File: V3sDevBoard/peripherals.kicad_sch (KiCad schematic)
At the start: 7 parts, among them Q1 NPN, Q2 PNP

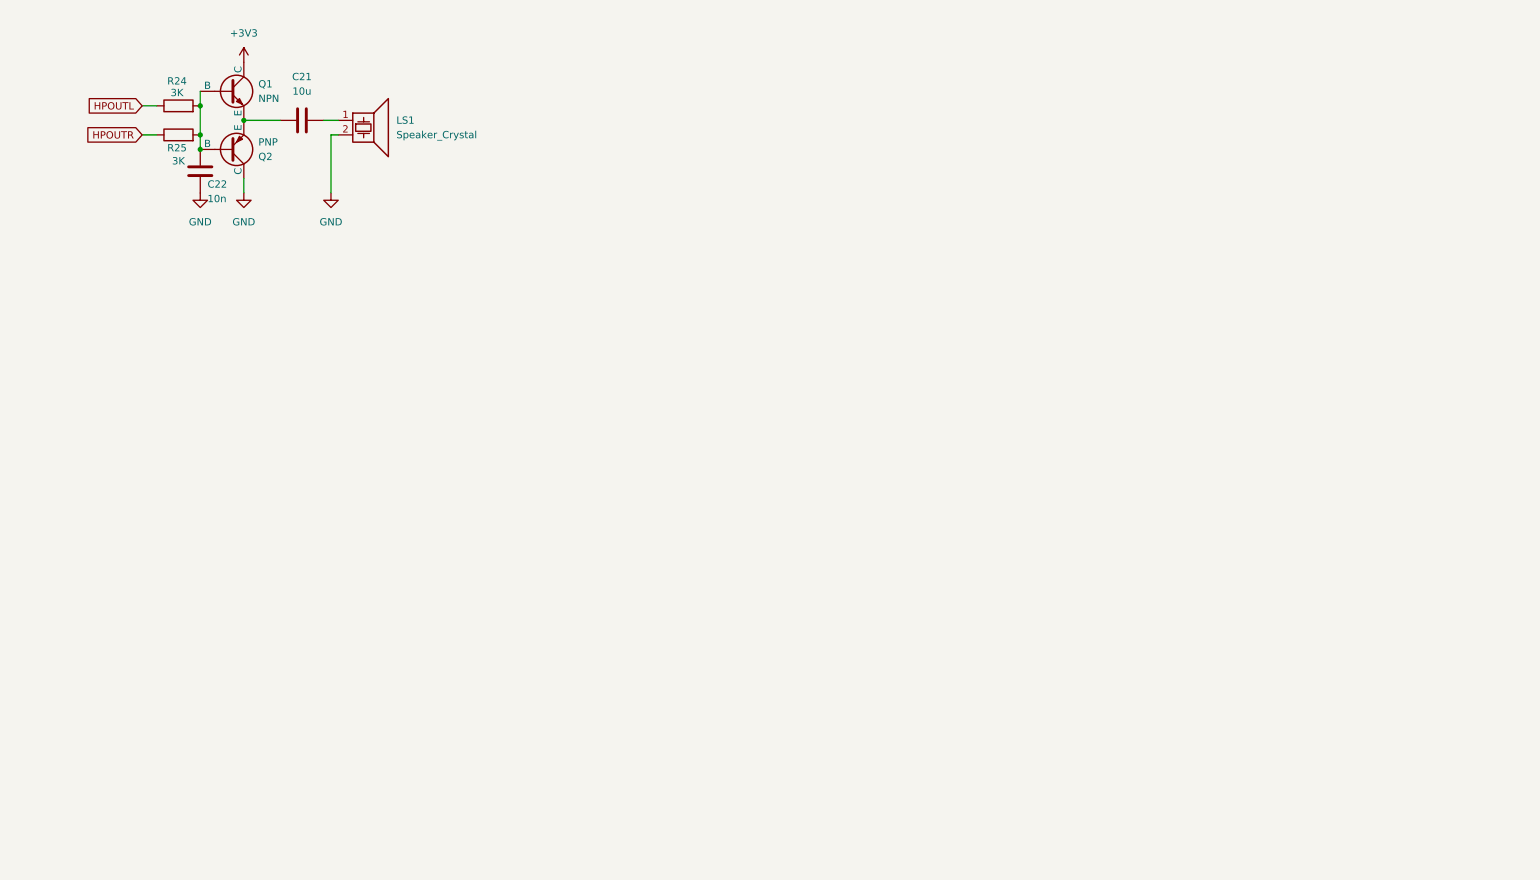
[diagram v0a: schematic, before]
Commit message: drawing schematics
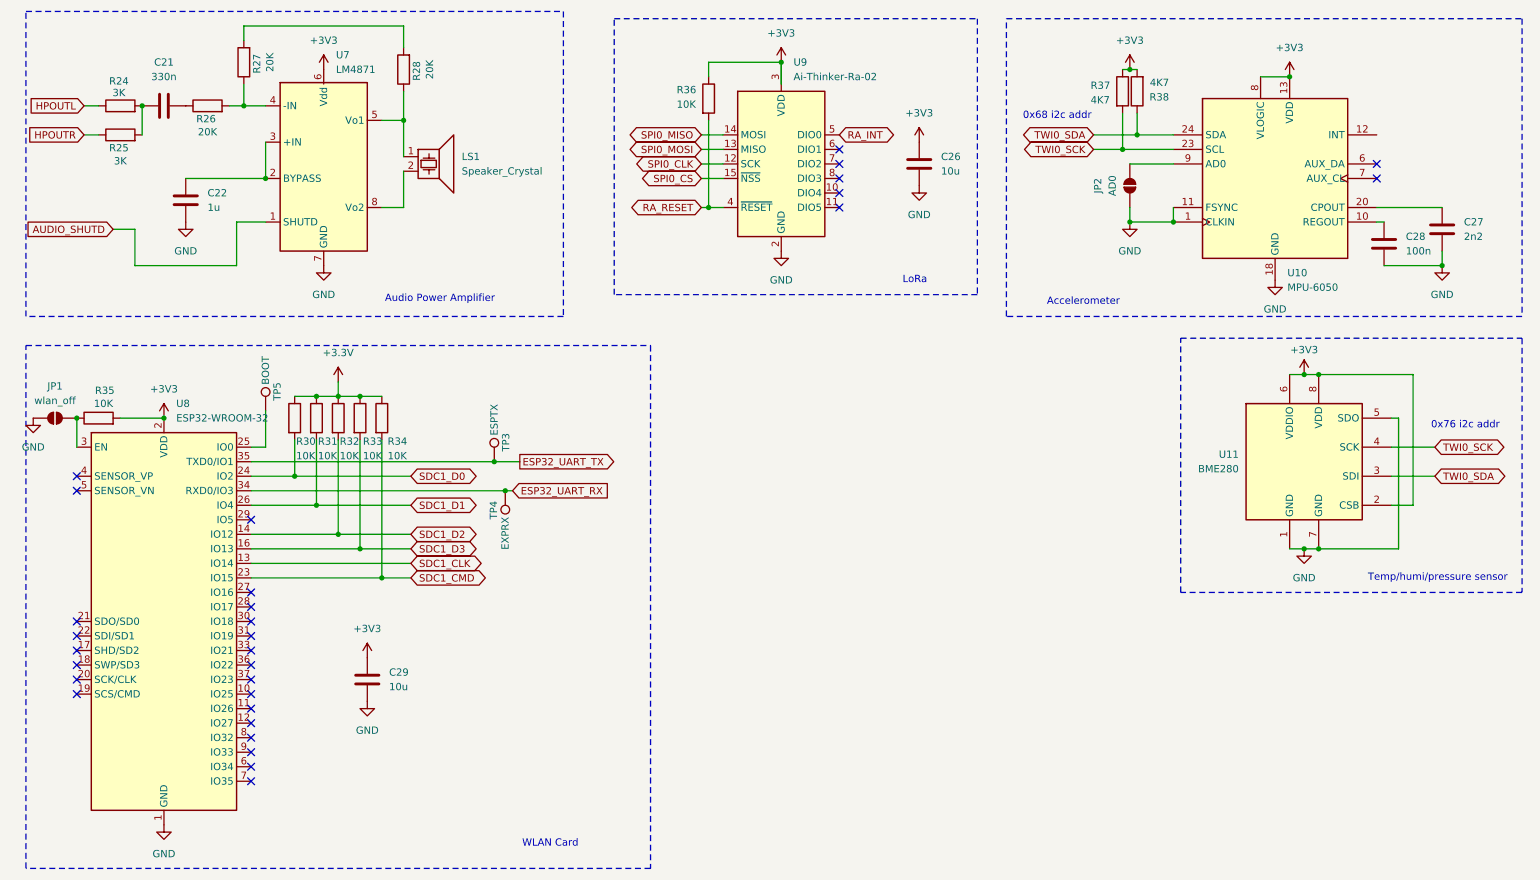
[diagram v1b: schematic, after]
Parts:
- removed Q1: NPN, Package_TO_SOT_SMD:SOT-23_Handsoldering, symbol Simulation_SPICE:NPN
- removed Q2: PNP, Package_TO_SOT_SMD:SOT-23_Handsoldering, symbol Simulation_SPICE:PNP
- added C26, C29: 10u, Capacitor_SMD:C_0805_2012Metric_Pad1.18x1.45mm_HandSolder, symbol Device:C
- added C27: 2n2, Capacitor_SMD:C_0805_2012Metric_Pad1.18x1.45mm_HandSolder, symbol Device:C
- added C28: 100n, Capacitor_SMD:C_0805_2012Metric_Pad1.18x1.45mm_HandSolder, symbol Device:C
- added JP1: wlan_off, Jumper:SolderJumper-2_P1.3mm_Open_RoundedPad1.0x1.5mm, symbol Jumper:SolderJumper_2_Open
- added JP2: AD0, Jumper:SolderJumper-2_P1.3mm_Open_RoundedPad1.0x1.5mm, symbol Jumper:SolderJumper_2_Open
- added R26, R27, R28: 20K, LED_SMD:LED_0805_2012Metric_Pad1.15x1.40mm_HandSolder, symbol Device:R
- added R30, R31, R32, R33, R34, R35, R36: 10K, Resistor_SMD:R_0805_2012Metric_Pad1.20x1.40mm_HandSolder, symbol Device:R
- added R37, R38: 4K7, Resistor_SMD:R_0805_2012Metric_Pad1.20x1.40mm_HandSolder, symbol Device:R
- added TP3: ESPTX, TestPoint:TestPoint_Pad_D1.0mm, symbol Connector:TestPoint
- added TP4: EXPRX, TestPoint:TestPoint_Pad_D1.0mm, symbol Connector:TestPoint
- added TP5: BOOT, TestPoint:TestPoint_Pad_D1.0mm, symbol Connector:TestPoint
- added U10: MPU-6050, Sensor_Motion:InvenSense_QFN-24_4x4mm_P0.5mm, symbol Sensor_Motion:MPU-6050
- added U11: BME280, Package_LGA:Bosch_LGA-8_2.5x2.5mm_P0.65mm_ClockwisePinNumbering, symbol Sensor:BME280
- added U7: LM4871, Package_SO:SOIC-8_5.3x6.2mm_P1.27mm, symbol Custom:LM4871
- added U8: ESP32-WROOM-32, RF_Module:ESP32-WROOM-32, symbol RF_Module:ESP32-WROOM-32
- added U9: Ai-Thinker-Ra-02, RF_Module:Ai-Thinker-Ra-01-LoRa, symbol RF_Module:Ai-Thinker-Ra-02
- C21: value 10u -> 330n
- C22: value 10n -> 1u
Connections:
- net +3V3: now also C26.1, C29.1, R35.2, R36.1, R37.1, R38.2, U10.13 (VDD), U10.8 (VLOGIC), U11.2 (CSB), U11.6 (VDDIO), U11.8 (VDD), U7.6 (Vdd), U8.2 (VDD), U9.3 (VDD)
- net GND: now also C26.2, C27.2, C28.2, C29.2, JP1.1 (A), JP2.1 (A), U10.1 (CLKIN), U10.11 (FSYNC), U10.18 (GND), U11.1 (GND), U11.5 (SDO), U11.7 (GND), U7.7 (GND), U8.1 (GND), U8.15 (GND), U8.38 (GND), U8.39 (GND), U9.1 (GND), U9.16 (GND), U9.2 (GND), U9.9 (GND); no longer LS1.2
- net at LS1.1: now also R28.1, U7.5 (Vo1); no longer C21.2
- net at R24.2, R25.2: now also C21.2; no longer C22.2
- net at C21.1: now also R26.1
- new net: C22.2, U7.2 (BYPASS), U7.3 (+IN)
- new net: R26.2, R27.1, U7.4 (-IN)
- new net: LS1.2, U7.8 (Vo2)
- new net: C28.1, U10.10 (REGOUT)
- new net: TP5.1, U8.25 (IO0)
- new net: JP1.2 (B), R35.1, U8.3 (EN)
- new net: R27.2, R28.2
- new net: JP2.2 (B), U10.9 (AD0)
- new net: C27.1, U10.20 (CPOUT)
- new net +3.3V: R30.1, R31.1, R32.1, R33.1, R34.1
- new net AUDIO_SHUTD: U7.1 (SHUTD)
- new net ESP32_UART_RX: TP4.1, U8.34 (RXD0/IO3)
- new net ESP32_UART_TX: TP3.1, U8.35 (TXD0/IO1)
- new net RA_INT: U9.5 (DIO0)
- new net RA_RESET: R36.2, U9.4 (~{RESET})
- new net SDC1_CLK: U8.13 (IO14)
- new net SDC1_CMD: R34.2, U8.23 (IO15)
- new net SDC1_D0: R30.2, U8.24 (IO2)
- new net SDC1_D1: R31.2, U8.26 (IO4)
- new net SDC1_D2: R32.2, U8.14 (IO12)
- new net SDC1_D3: R33.2, U8.16 (IO13)
- new net SPI0_CLK: U9.12 (SCK)
- new net SPI0_CS: U9.15 (~{NSS})
- new net SPI0_MISO: U9.14 (MOSI)
- new net SPI0_MOSI: U9.13 (MISO)
- new net TWI0_SCK: R37.2, U10.23 (SCL), U11.4 (SCK)
- new net TWI0_SDA: R38.1, U10.24 (SDA), U11.3 (SDI)
- no-connect marks 0 -> 30
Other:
- note added: "0x68 i2c addr"
- note added: "0x76 i2c addr"
- note added: "Accelerometer"
- note added: "Audio Power Amplifier"
- note added: "LoRa"
- note added: "Temp/humi/pressure sensor"
- note added: "WLAN Card"
- company: (none) -> J.K.
- title: (none) -> V3s Dev Board
- moved on the sheet: LS1, R24, R25

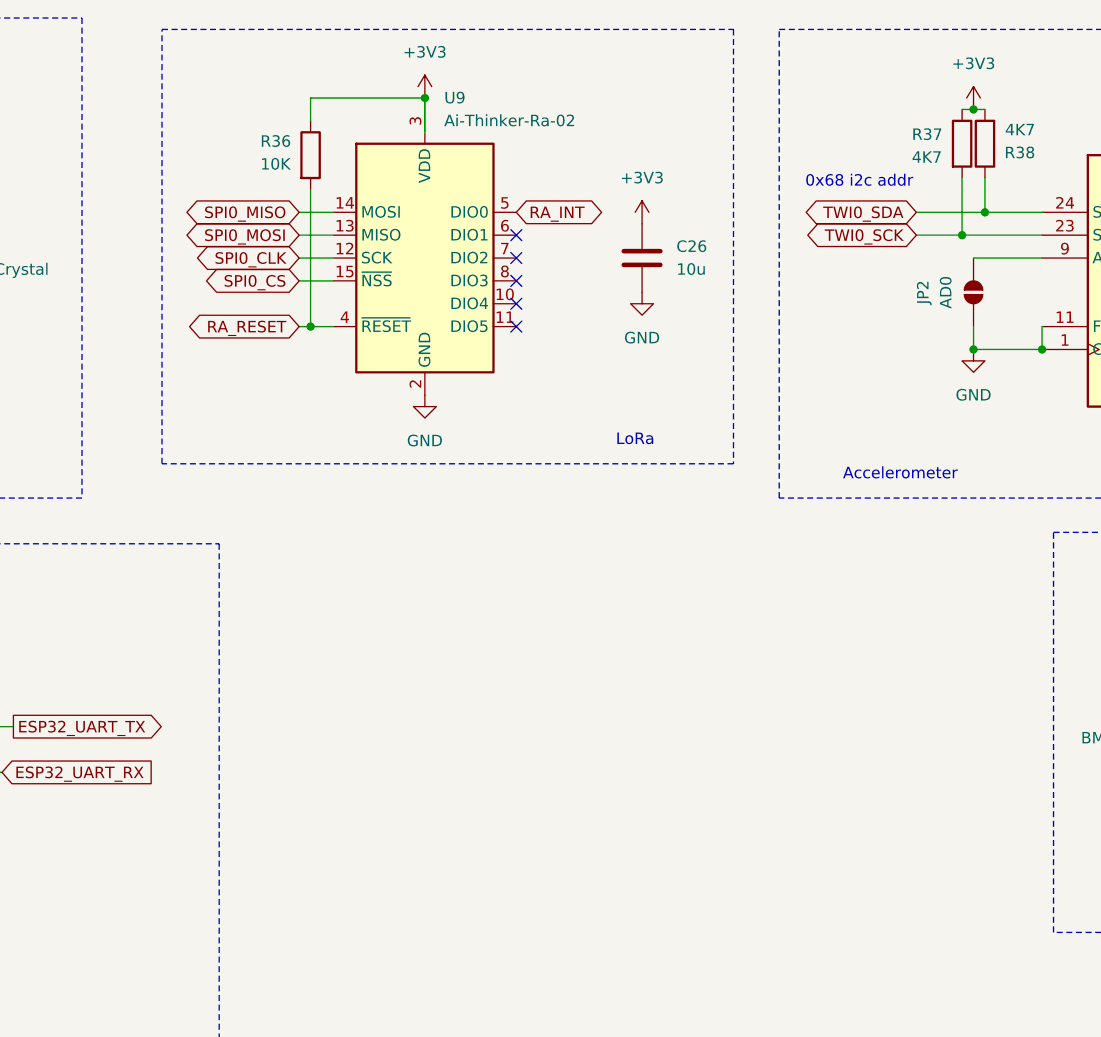
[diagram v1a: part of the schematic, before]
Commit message: advancing in schematics and footprints
Making needed custom footprints for connectors, adding a lot of small changes to schematics.
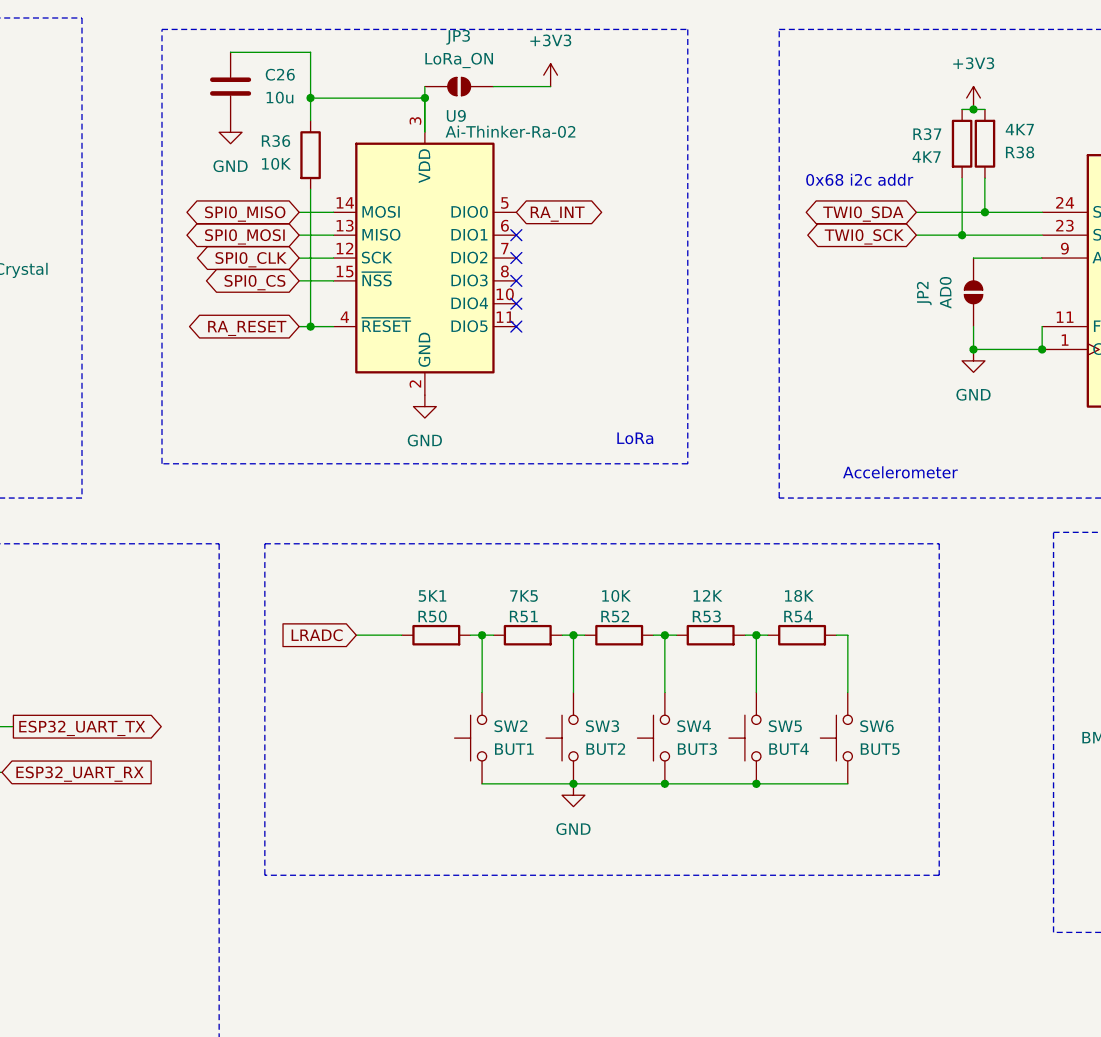
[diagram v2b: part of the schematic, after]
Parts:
- added JP3: LoRa_ON, Jumper:SolderJumper-2_P1.3mm_Open_RoundedPad1.0x1.5mm, symbol Jumper:SolderJumper_2_Open
- added R50: 5K1, Resistor_SMD:R_0805_2012Metric_Pad1.20x1.40mm_HandSolder, symbol Device:R
- added R51: 7K5, Resistor_SMD:R_0805_2012Metric_Pad1.20x1.40mm_HandSolder, symbol Device:R
- added R52: 10K, Resistor_SMD:R_0805_2012Metric_Pad1.20x1.40mm_HandSolder, symbol Device:R
- added R53: 12K, Resistor_SMD:R_0805_2012Metric_Pad1.20x1.40mm_HandSolder, symbol Device:R
- added R54: 18K, Resistor_SMD:R_0805_2012Metric_Pad1.20x1.40mm_HandSolder, symbol Device:R
- added SW2: BUT1, Button_Switch_THT:SW_PUSH_6mm, symbol Switch:SW_Push
- added SW3: BUT2, Button_Switch_THT:SW_PUSH_6mm, symbol Switch:SW_Push
- added SW4: BUT3, Button_Switch_THT:SW_PUSH_6mm, symbol Switch:SW_Push
- added SW5: BUT4, Button_Switch_THT:SW_PUSH_6mm, symbol Switch:SW_Push
- added SW6: BUT5, Button_Switch_THT:SW_PUSH_6mm, symbol Switch:SW_Push
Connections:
- net +3V3: now also JP3.2 (B); no longer C26.1, R36.1, U9.3 (VDD)
- net GND: now also SW2.1, SW3.1, SW4.1, SW5.1, SW6.1
- new net: C26.1, JP3.1 (A), R36.1, U9.3 (VDD)
- new net: R51.2, R52.1, SW3.2
- new net: R52.2, R53.1, SW4.2
- new net: R53.2, R54.1, SW5.2
- new net: R54.2, SW6.2
- new net: R50.2, R51.1, SW2.2
- new net LRADC: R50.1
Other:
- title: V3s Dev Board -> V3s_Dev_Board
- moved on the sheet: C26

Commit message: completing schematics
completing schematics, adding netclasses, fixing bugs, updating readme, starting pcb
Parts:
- removed C22: 1u, Capacitor_SMD:C_0805_2012Metric_Pad1.18x1.45mm_HandSolder, symbol Device:C
- removed JP2: AD0, Jumper:SolderJumper-2_P1.3mm_Open_RoundedPad1.0x1.5mm, symbol Jumper:SolderJumper_2_Open
- removed JP3: LoRa_ON, Jumper:SolderJumper-2_P1.3mm_Open_RoundedPad1.0x1.5mm, symbol Jumper:SolderJumper_2_Open
- removed LS1: Speaker_Crystal, symbol Device:Speaker_Crystal
- removed U7: LM4871, Package_SO:SOIC-8_5.3x6.2mm_P1.27mm, symbol Custom:LM4871
- added C45: 100n, Capacitor_SMD:C_0805_2012Metric_Pad1.18x1.45mm_HandSolder, symbol Device:C
- added C47: 1n, Capacitor_SMD:C_0805_2012Metric_Pad1.18x1.45mm_HandSolder, symbol Device:C_Small
- added D12: LED-B, LED_SMD:LED_0805_2012Metric_Pad1.15x1.40mm_HandSolder, symbol Device:LED
- added J9: GPIO, Connector_PinHeader_2.54mm:PinHeader_1x10_P2.54mm_Vertical, symbol Connector:Conn_01x10_Pin
- added JP2: ADRES, Jumper:SolderJumper-2_P1.3mm_Bridged_RoundedPad1.0x1.5mm, symbol Jumper:SolderJumper_2_Bridged
- added JP3: pwr, Jumper:SolderJumper-2_P1.3mm_Bridged_RoundedPad1.0x1.5mm, symbol Jumper:SolderJumper_2_Bridged
- added R57, R59: 10K, Resistor_SMD:R_0603_1608Metric_Pad0.98x0.95mm_HandSolder, symbol Device:R
- added R60: 33K, Resistor_SMD:R_0805_2012Metric_Pad1.20x1.40mm_HandSolder, symbol Device:R
- added R61, R62, R71, R72: 150R, Resistor_SMD:R_0805_2012Metric_Pad1.20x1.40mm_HandSolder, symbol Device:R
- added R68: 100K, Resistor_SMD:R_0805_2012Metric_Pad1.20x1.40mm_HandSolder, symbol Device:R
- added SW1: BUT6, Button_Switch_THT:SW_PUSH_6mm, symbol Switch:SW_Push
- C21: value 330n -> 100n
- C26, C29: footprint Capacitor_SMD:C_0805_2012Metric_Pad1.18x1.45mm_HandSolder -> Capacitor_SMD:C_1206_3216Metric
- R24, R25: value 3K -> 150R; footprint LED_SMD:LED_0805_2012Metric_Pad1.15x1.40mm_HandSolder -> Resistor_SMD:R_0805_2012Metric_Pad1.20x1.40mm_HandSolder; now not fitted
- R26, R27, R28: value 20K -> 150R; footprint LED_SMD:LED_0805_2012Metric_Pad1.15x1.40mm_HandSolder -> Resistor_SMD:R_0805_2012Metric_Pad1.20x1.40mm_HandSolder; now not fitted
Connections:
- net HPOUTL is gone; now on net SPI0_MOSI: R24.1
- net HPOUTR is gone; now on net SPI0_CS: R25.1
- net +3.3V: now also C21.2, C29.1, R35.2, R37.1, R38.2, U10.13 (VDD), U10.8 (VLOGIC), U11.6 (VDDIO), U11.8 (VDD), U8.2 (VDD), C45.2, J9.9 (Pin_9), JP3.1 (A), R59.1, R68.1
- net ESP32_UART_RX: now also R72.2; no longer TP4.1, U8.34 (RXD0/IO3)
- net ESP32_UART_TX: now also R71.1; no longer TP3.1, U8.35 (TXD0/IO1)
- net GND: now also C21.1, C45.1, C47.2, D12.1 (K), J9.10 (Pin_10), JP2.2 (B), R57.2, SW1.1; no longer U11.5 (SDO)
- net LRADC: now also C47.1, D12.2 (A), R68.2
- net SPI0_CLK: now also R26.1
- net SPI0_MISO: now also R27.1
- net at R26.2: now also J9.3 (Pin_3); no longer R27.1
- net PF6: now reaches R28.1
- net at C26.1, R36.1, U9.3 (VDD): now also JP3.2 (B)
- net at R54.2, SW6.2: now also R60.1
- net at R28.2: now also J9.5 (Pin_5); no longer R27.2
- net at U10.9 (AD0): now also JP2.1 (A)
- removed net +3V3: C29.1, R35.2, R37.1, R38.2, U10.13 (VDD), U10.8 (VLOGIC), U11.2 (CSB), U11.6 (VDDIO), U11.8 (VDD), U8.2 (VDD)
- new net: R72.1, TP4.1, U8.34 (RXD0/IO3)
- new net: R60.2, SW1.2
- new net: R71.2, TP3.1, U8.35 (TXD0/IO1)
- new net: R59.2, U11.2 (CSB)
- new net: J9.1 (Pin_1), R24.2
- new net: J9.2 (Pin_2), R25.2
- new net: J9.4 (Pin_4), R27.2
- new net: J9.6 (Pin_6), R61.2
- new net: J9.7 (Pin_7), R62.2
- new net: R57.1, U11.5 (SDO)
- new net CSI_SCK: R62.1
- new net CSI_SDA: R61.1
- new net VCC: J9.8 (Pin_8)
- no-connect marks 30 -> 31
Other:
- note added: "GPIO"
- note added: "Keypad"
- note removed: "Audio Power Amplifier"
- company: J.K. -> jakub.kmiecik@protonmail.com
- moved on the sheet: C26, C27, C28, C29, JP1, R30, R31, R32, R33, R34, R35, R36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
